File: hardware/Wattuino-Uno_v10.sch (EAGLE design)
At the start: 61 parts, among them IC1 ATMEGA328-PU, IC2 FT231XQ, IC3 LDO-TS1117CW-5V, IC4 LDO-TS9011-3V3, J2 USB-B-H, J3 USB-MICRO, Q1 16MHz, X1 PASSER-07, X2 PASSER-07, X3 PASSER-07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

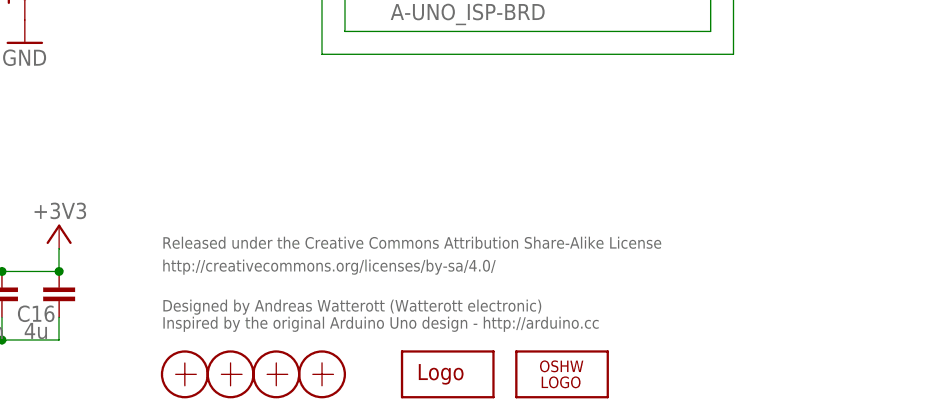
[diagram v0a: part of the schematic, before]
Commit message: updated schematics
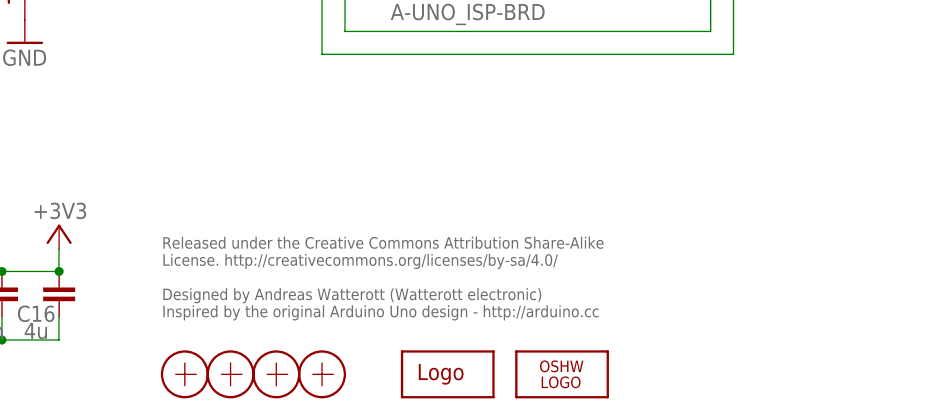
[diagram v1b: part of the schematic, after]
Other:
- note added: "Released under the Creative Commons Attribution Share-Alike License. http://creativecommons.org/licenses/by-sa/4.0/ Designed by Andreas Watterott (Watterott electronic) Inspired by the original Arduino Uno design - http://arduino.cc"
- note removed: "Designed by Andreas Watterott (Watterott electronic) Inspired by the original Arduino Uno design - http://arduino.cc"
- note removed: "Released under the Creative Commons Attribution Share-Alike License"
- note removed: "http://creativecommons.org/licenses/by-sa/4.0/"
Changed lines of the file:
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@@
 <?xml version="1.0" encoding="utf-8"?>
 <!DOCTYPE eagle SYSTEM "eagle.dtd">
-<eagle version="7.2.0">
+<eagle version="7.5.0">
 <drawing>
 <settings>
@@
 <sheet>
 <plain>
-<text x="162.56" y="21.59" size="1.27" layer="95">Released under the Creative Commons Attribution Share-Alike License</text>
-<text x="162.56" y="19.05" size="1.27" layer="95">http://creativecommons.org/licenses/by-sa/4.0/</text>
-<text x="162.56" y="12.7" size="1.27" layer="95">Designed by Andreas Watterott (Watterott electronic)
+<text x="162.56" y="22.86" size="1.27" layer="95" align="top-left">Released under the Creative Commons Attribution Share-Alike
+License. http://creativecommons.org/licenses/by-sa/4.0/
+Designed by Andreas Watterott (Watterott electronic)
 Inspired by the original Arduino Uno design - http://arduino.cc</text>
 <text x="73.66" y="161.29" size="3.81" layer="97">ATmega328</text>

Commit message: updated schematics
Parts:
- L1: value (none) -> 10u
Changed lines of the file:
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@@
 <setting verticaltext="up"/>
 </settings>
-<grid distance="0.05" unitdist="inch" unit="inch" style="lines" multiple="1" display="yes" altdistance="0.025" altunitdist="inch" altunit="inch"/>
+<grid distance="0.1" unitdist="inch" unit="inch" style="lines" multiple="1" display="no" altdistance="0.01" altunitdist="inch" altunit="inch"/>
 <layers>
 <layer number="1" name="Top" color="4" fill="1" visible="no" active="no"/>
@@
 <part name="C17" library="we-rcl" deviceset="CAPACITOR" device="-0402" value="100n"/>
 <part name="C18" library="we-rcl" deviceset="CAPACITOR" device="-1206" value="10u"/>
-<part name="L1" library="we-rcl" deviceset="INDUCTOR" device="-0603"/>
+<part name="L1" library="we-rcl" deviceset="INDUCTOR" device="-0603" value="10u"/>
 <part name="P+10" library="supply1" deviceset="+5V" device=""/>
 <part name="+3V5" library="supply1" deviceset="+3V3" device=""/>
